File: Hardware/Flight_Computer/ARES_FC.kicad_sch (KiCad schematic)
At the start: 65 parts, among them J1 SWD, J2 TYPE-C-31-M-12, J3 FC_M/P, J4 5V, J5 GND, J6 FC_RF, J7 Conn_01x04_Pin, J8 Conn_01x04_Pin, U1 STM32F401CCU6, U2 AMS1117-3.3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

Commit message: aesthetic edits (silkscreen, etc.)
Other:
- note removed: "double-check FB"
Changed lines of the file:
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@@
-		)
-	)
-	(text "double-check FB"
-		(exclude_from_sim no)
-		(at 290.83 101.6 0)
-		(effects
-			(font
-				(size 1.27 1.27)
-			)
 		)
 	)

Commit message: connected GPS_NRST to STM32
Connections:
- net NRESET is gone; now on net GPS_NRST: R5.2, U6.2 (NRESET)
- net GPS_NRST: now reaches U1.42 (PB6)
- no-connect marks 20 -> 19
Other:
- moved on the sheet: C23, C24, U3

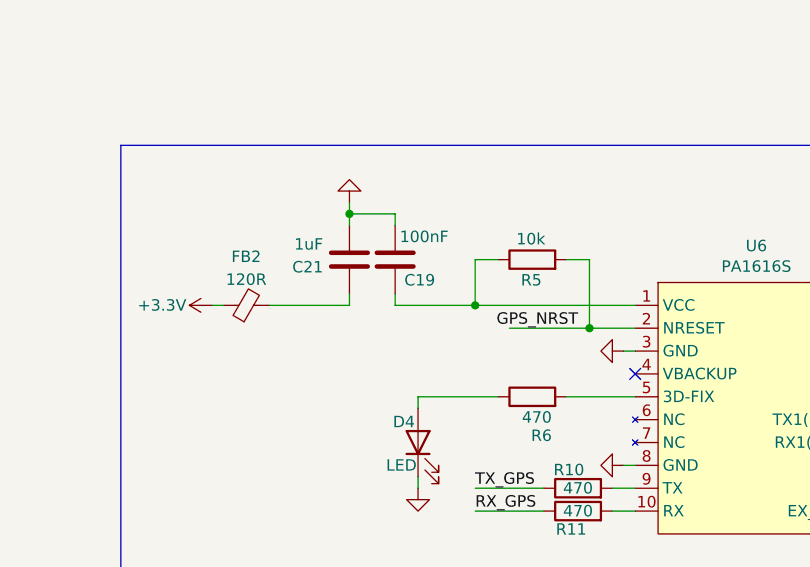
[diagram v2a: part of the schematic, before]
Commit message: some LCSC Part (BOM) changes; more needed.
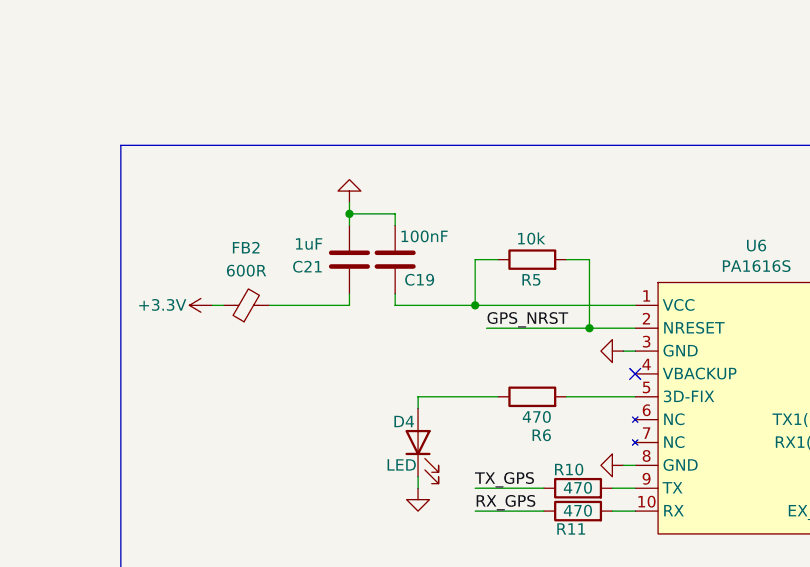
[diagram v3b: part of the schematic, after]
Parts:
- AE1: LCSC Part (none) -> C5137195
- FB2: value 120R -> 600R; LCSC Part C85831 -> C88976
- J3, J6: LCSC Part C505273 -> C132510
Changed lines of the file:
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@@
 	(wire
 		(pts
-			(xy 323.85 113.03) (xy 332.74 113.03)
+			(xy 321.31 113.03) (xy 332.74 113.03)
 		)
 		(stroke
@@
 	(wire
 		(pts
+			(xy 76.2 109.22) (xy 86.36 109.22)
+		)
+		(stroke
+			(width 0)
+			(type default)
+		)
+	)
+	(wire
+		(pts
 			(xy 311.15 53.34) (xy 320.04 53.34)
 		)
@@
 	(wire
 		(pts
-			(xy 76.2 109.22) (xy 86.36 109.22)
-		)
-		(stroke
-			(width 0)
-			(type default)
-		)
-	)
-	(wire
-		(pts
 			(xy 37.592 39.37) (xy 37.592 36.83)
 		)
@@
 		)
 	)
-	(label "GPS_NRST"
-		(at 76.2 109.22 0)
-		(fields_autoplaced yes)
-		(effects
-			(font
-				(size 1.27 1.27)
-			)
-			(justify left bottom)
-		)
-	)
 	(label "USB_D-"
 		(at 128.778 119.38 180)
@@
 	)
 	(label "GPS_NRST"
-		(at 331.47 113.03 180)
+		(at 321.31 113.03 0)
 		(fields_autoplaced yes)
 		(effects
@@
 				(size 1.27 1.27)
 			)
-			(justify right bottom)
+			(justify left bottom)
 		)
 	)
@@
 		)
 	)
+	(label "GPS_NRST"
+		(at 76.2 109.22 0)
+		(fields_autoplaced yes)
+		(effects
+			(font
+				(size 1.27 1.27)
+			)
+			(justify left bottom)
+		)
+	)
 	(label "SDA"
 		(at 241.3 160.02 0)
@@
 			)
 		)
-		(property "LCSC Part" "C505273"
+		(property "LCSC Part" "C132510"
 			(at 53.34 190.5 0)
 			(effects
@@
 			)
 		)
+		(property "LCSC Part" "C5137195"
+			(at 373.38 133.35 90)
+			(effects
+				(font
+					(size 1.27 1.27)
+				)
+				(hide yes)
+			)
+		)
 		(pin "1"
 		)
@@
 		(fields_autoplaced yes)
 		(property "Reference" "FB2"
-			(at 294.6019 105.0884 90)
+			(at 294.6019 104.14 90)
 			(effects
 				(font
@@
 			)
 		)
-		(property "Value" "120R"
-			(at 294.6019 107.6253 90)
+		(property "Value" "600R"
+			(at 294.6019 106.68 90)
 			(effects
 				(font
@@
 			)
 		)
-		(property "LCSC Part" "C85831"
+		(property "LCSC Part" "C88976"
 			(at 294.64 110.49 0)
 			(effects
@@
 			)
 		)
-		(property "LCSC Part" "C505273"
+		(property "LCSC Part" "C132510"
 			(at 78.74 190.5 0)
 			(effects

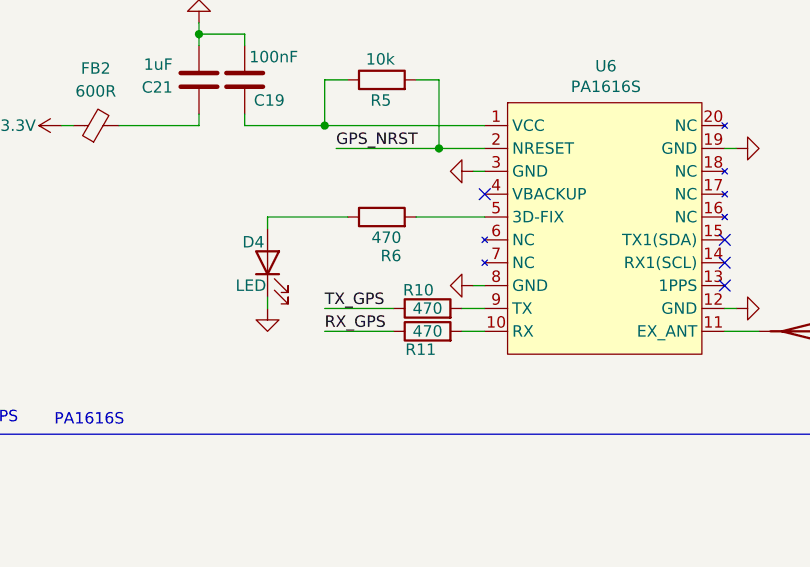
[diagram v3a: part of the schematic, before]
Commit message: fixed JLC part numbers and ran DRC
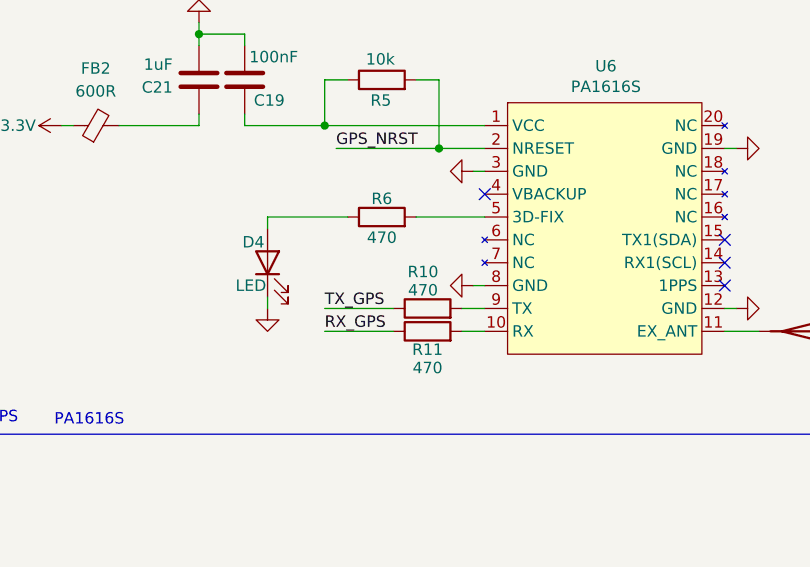
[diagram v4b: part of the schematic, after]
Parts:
- C4: footprint Capacitor_SMD:C_0402_1005Metric -> Capacitor_SMD:C_0603_1608Metric
- D1, D2: LCSC Part C273598 -> C12624
- D3: LCSC Part C273598 -> C2288
- D4: LCSC Part C273598 -> C2290
- J7, J8: LCSC Part (none) -> C160390
- R10, R11, R6: LCSC Part C11702 -> 0402WGJ0471TCE
- U6: LCSC Part (none) -> C9900146965
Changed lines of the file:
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@@
 			)
 		)
-		(property "Description" ""
+		(property "Description" "GPS Module"
+			(at 340.36 107.95 0)
+			(effects
+				(font
+					(size 1.27 1.27)
+				)
+				(hide yes)
+			)
+		)
+		(property "LCSC Part" "C9900146965"
 			(at 340.36 107.95 0)
 			(effects
@@
 			)
 		)
-		(property "LCSC Part" "C273598"
+		(property "LCSC Part" "C2290"
 			(at 313.69 125.73 0)
 			(effects
@@
 		(dnp no)
 		(property "Reference" "R10"
-			(at 330.454 128.778 90)
+			(at 330.962 126.746 90)
 			(effects
 				(font
@@
 		)
 		(property "Value" "470"
-			(at 331.47 130.81 90)
+			(at 330.962 128.778 90)
 			(effects
 				(font
@@
 			)
 		)
-		(property "LCSC Part" "C11702"
+		(property "LCSC Part" "0402WGJ0471TCE "
 			(at 331.47 130.81 0)
 			(effects
@@
 			)
 		)
-		(property "Footprint" "Capacitor_SMD:C_0402_1005Metric"
+		(property "Footprint" "Capacitor_SMD:C_0603_1608Metric"
 			(at 38.5572 46.99 0)
 			(effects
@@
 			)
 		)
-		(property "LCSC Part" "C273598"
+		(property "LCSC Part" "C12624"
 			(at 132.588 182.88 0)
 			(effects
@@
 			)
 		)
-		(property "LCSC Part" "C273598"
+		(property "LCSC Part" "C12624"
 			(at 232.918 33.274 0)
 			(effects
@@
 			)
 		)
+		(property "LCSC Part" "C160390"
+			(at 252.73 160.02 0)
+			(effects
+				(font
+					(size 1.27 1.27)
+				)
+				(hide yes)
+			)
+		)
 		(pin "1"
 		)
@@
 			)
 		)
-		(property "LCSC Part" "C273598"
+		(property "LCSC Part" "C2288"
 			(at 137.668 182.88 0)
 			(effects
@@
 		(dnp no)
 		(property "Reference" "R6"
-			(at 327.406 124.968 90)
+			(at 326.39 118.618 90)
 			(effects
 				(font
@@
 		)
 		(property "Value" "470"
-			(at 326.898 122.936 90)
+			(at 326.39 122.936 90)
 			(effects
 				(font
@@
 			)
 		)
-		(property "LCSC Part" "C11702"
+		(property "LCSC Part" "0402WGJ0471TCE"
 			(at 326.39 120.65 0)
 			(effects
@@
 		(dnp no)
 		(property "Reference" "R11"
-			(at 330.708 135.382 90)
+			(at 331.47 135.382 90)
 			(effects
 				(font
@@
 		)
 		(property "Value" "470"
-			(at 331.47 133.35 90)
+			(at 331.47 137.414 90)
 			(effects
 				(font
@@
 			)
 		)
-		(property "LCSC Part" "C11702"
+		(property "LCSC Part" "0402WGJ0471TCE "
 			(at 331.47 133.35 0)
 			(effects
@@
 			(at 252.73 172.72 0)
 			(effects
+				(font
+					(size 1.27 1.27)
+				)
+				(hide yes)
+			)
+		)
+		(property "LCSC Part" "C160390"
+			(at 252.73 172.72 0)
+			(effects

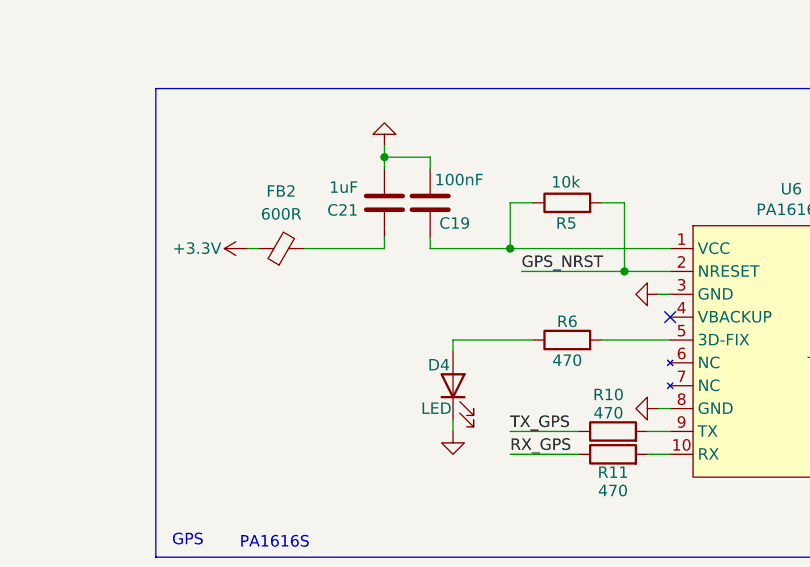
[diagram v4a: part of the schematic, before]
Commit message: added missing 3.3V bridge connection to GPS PS pin
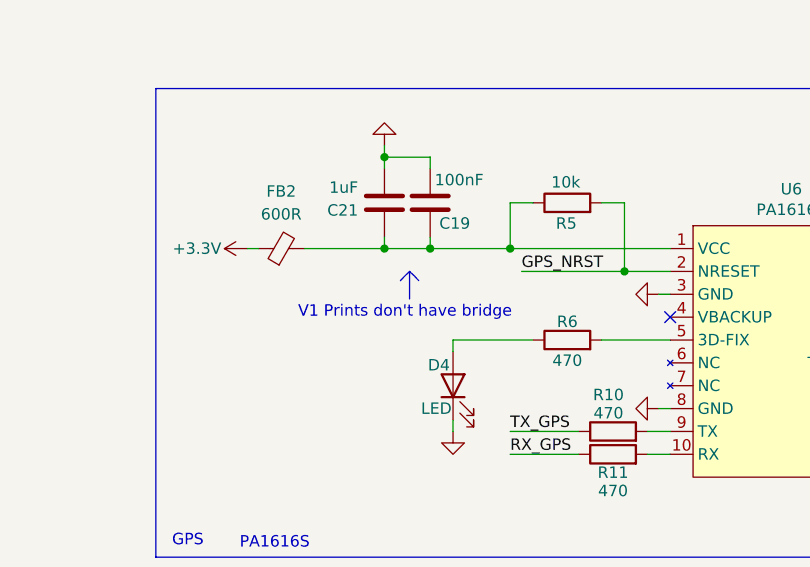
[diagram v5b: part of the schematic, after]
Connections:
- net at C19.1, R5.1, U6.1 (VCC): now also C21.1, FB2.2
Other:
- note added: "V1 Prints don't have bridge"
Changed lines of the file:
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@@
 	)
 	(junction
+		(at 311.15 110.49)
+		(diameter 0)
+		(color 0 0 0 0)
+	)
+	(junction
 		(at 346.456 204.47)
 		(diameter 0)
@@
 	)
 	(junction
+		(at 306.07 110.49)
+		(diameter 0)
+		(color 0 0 0 0)
+	)
+	(junction
 		(at 362.458 204.47)
 		(diameter 0)
@@
 	(polyline
 		(pts
+			(xy 308.862 113.034) (xy 308.862 113.542)
+		)
+		(stroke
+			(width 0)
+			(type default)
+		)
+	)
+	(polyline
+		(pts
 			(xy 183.134 202.438) (xy 183.134 243.078)
 		)
@@
 	(wire
 		(pts
+			(xy 306.07 110.49) (xy 311.15 110.49)
+		)
+		(stroke
+			(width 0)
+			(type default)
+		)
+	)
+	(wire
+		(pts
 			(xy 297.18 55.88) (xy 297.18 58.42)
 		)
@@
 		)
 	)
+	(polyline
+		(pts
+			(xy 308.862 113.542) (xy 308.862 116.082)
+		)
+		(stroke
+			(width 0)
+			(type default)
+		)
+	)
 	(wire
 		(pts
@@
 		)
 	)
+	(arc
+		(start 307.848 114.054)
+		(mid 308.3372 113.5272)
+		(end 308.864 113.038)
+		(stroke
+			(width 0)
+			(type default)
+		)
+		(fill
+			(type none)
+		)
+	)
+	(arc
+		(start 308.862 113.034)
+		(mid 309.3887 113.5233)
+		(end 309.878 114.05)
+		(stroke
+			(width 0)
+			(type default)
+		)
+		(fill
+			(type none)
+		)
+	)
 	(rectangle
 		(start 280.67 92.71)
@@
 		)
 	)
+	(text "V1 Prints don't have bridge"
+		(exclude_from_sim no)
+		(at 308.354 117.606 0)
+		(effects
+			(font
+				(size 1.27 1.27)
+			)
+		)
+	)
 	(text "1x 100nF per VDD pin"
 		(exclude_from_sim no)
@@
 		)
 		(instances
-			(project ""
+			(project "ARES_FC"
 				(path "/449acbee-2eeb-4316-a8e9-c26dd430524e"
 					(reference "J7")
